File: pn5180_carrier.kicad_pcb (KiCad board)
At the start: 2 copper layers, 62.5 x 106.5 mm, 35 parts, among them J1 Bay 0 (CLIK-Mate 1x10), J10 24V IN (CLIK-Mate 1x2), J2 Bay 1 (CLIK-Mate 1x10), J3 Bay 2 (CLIK-Mate 1x10), J4 Bay 3 (CLIK-Mate 1x10), J5 Bay 4 (CLIK-Mate 1x10), J6 Bay 5 (CLIK-Mate 1x10), J7 Bay 6 (CLIK-Mate 1x10), J8 Bay 7 (CLIK-Mate 1x10), U1 74HC138, U2 74HC151, U4 TLV1117LV33DCYR, U5 XIAO ESP32C6, U6 MP1584EN module (set 5.0V)

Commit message: PCB: J1-J8 swapped to the 2x5 CLIK-Mate footprint (Update PCB from Schematic, KiCad GUI)
Same positions and orientations as the 1x10 parts; tracks to the bay connectors
still need re-routing. Project file records schematic rev 1.4.

Co-Authored-By: Claude Fable 5.1 <noreply@anthropic.com>
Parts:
- J1: value Bay 0 (CLIK-Mate 1x10) -> Bay 0 (CLIK-Mate 2x5); footprint Connector_Molex:Molex_CLIK-Mate_502494-1070_1x10-1MP_P2.00mm_Horizontal -> carrier:Molex_CLIK-Mate_503148-1090_2x05-1MP_P1.50mm_Horizontal
- J2: value Bay 1 (CLIK-Mate 1x10) -> Bay 1 (CLIK-Mate 2x5); footprint Connector_Molex:Molex_CLIK-Mate_502494-1070_1x10-1MP_P2.00mm_Horizontal -> carrier:Molex_CLIK-Mate_503148-1090_2x05-1MP_P1.50mm_Horizontal
- J3: value Bay 2 (CLIK-Mate 1x10) -> Bay 2 (CLIK-Mate 2x5); footprint Connector_Molex:Molex_CLIK-Mate_502494-1070_1x10-1MP_P2.00mm_Horizontal -> carrier:Molex_CLIK-Mate_503148-1090_2x05-1MP_P1.50mm_Horizontal
- J4: value Bay 3 (CLIK-Mate 1x10) -> Bay 3 (CLIK-Mate 2x5); footprint Connector_Molex:Molex_CLIK-Mate_502494-1070_1x10-1MP_P2.00mm_Horizontal -> carrier:Molex_CLIK-Mate_503148-1090_2x05-1MP_P1.50mm_Horizontal
- J5: value Bay 4 (CLIK-Mate 1x10) -> Bay 4 (CLIK-Mate 2x5); footprint Connector_Molex:Molex_CLIK-Mate_502494-1070_1x10-1MP_P2.00mm_Horizontal -> carrier:Molex_CLIK-Mate_503148-1090_2x05-1MP_P1.50mm_Horizontal
- J6: value Bay 5 (CLIK-Mate 1x10) -> Bay 5 (CLIK-Mate 2x5); footprint Connector_Molex:Molex_CLIK-Mate_502494-1070_1x10-1MP_P2.00mm_Horizontal -> carrier:Molex_CLIK-Mate_503148-1090_2x05-1MP_P1.50mm_Horizontal
- J7: value Bay 6 (CLIK-Mate 1x10) -> Bay 6 (CLIK-Mate 2x5); footprint Connector_Molex:Molex_CLIK-Mate_502494-1070_1x10-1MP_P2.00mm_Horizontal -> carrier:Molex_CLIK-Mate_503148-1090_2x05-1MP_P1.50mm_Horizontal
- J8: value Bay 7 (CLIK-Mate 1x10) -> Bay 7 (CLIK-Mate 2x5); footprint Connector_Molex:Molex_CLIK-Mate_502494-1070_1x10-1MP_P2.00mm_Horizontal -> carrier:Molex_CLIK-Mate_503148-1090_2x05-1MP_P1.50mm_Horizontal
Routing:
- net MOSI: track 211.4 -> 114.7 mm, vias 12 -> 6
- net MISO: track 211.8 -> 300.3 mm, vias 12 -> 14
- net +3V3: track 426.7 -> 404.5 mm, vias 15 -> 10
- net BUSY5: track 36.8 -> 19.3 mm, vias 2 -> 1
- net +5V: track 437.4 -> 424.5 mm
- net NSS5: track 16.5 -> 8.94 mm, vias 2 -> 0
- net ~{RST}: track 246.5 -> 241.3 mm, vias 6 -> 4
- net SCK: track 193.3 -> 190.3 mm
- net GND: vias 43 -> 37

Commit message: 3D models for the parts KiCad ships none for; preview render and tools
- carrier.3dshapes/: simplified VRML models generated by tools/gen_3d_models.py —
  CLIK-Mate 503148-1090 2x5 and 502494-0270 1x2 receptacles, XIAO ESP32C6 on its two
  8.5 mm sockets (rounded board, castellations, USB-C, shield, u.FL, chip antenna,
  buttons), MP1584EN module, Littelfuse NANO2 fuse
- carrier.pretty: model references on the three custom footprints; project-local
  copies of the stock J10 and F1 footprints that differ only in the model path;
  schematic/BOM/README point J10 and F1 at carrier:
- PCB: model references text-patched into the embedded footprints (all 35 resolve);
  otherwise identical to the owner's a606ea7 save
- tools/: footprint and model generators, render_3d_preview.py (kicad-cli pcb render on
  a temp copy); pn5180_carrier_3d_preview.png; renders/ ignored
- README/CLAUDE.md/MEMORY.md: files, tooling, conventions, PCB status, item 13

Co-Authored-By: Claude Fable 5.1 <noreply@anthropic.com>
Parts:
- F1: footprint Fuse:Fuse_Littelfuse-NANO2-451_453 -> carrier:Fuse_Littelfuse-NANO2-451_453
- J10: footprint Connector_Molex:Molex_CLIK-Mate_502494-0270_1x02-1MP_P2.00mm_Horizontal -> carrier:Molex_CLIK-Mate_502494-0270_1x02-1MP_P2.00mm_Horizontal
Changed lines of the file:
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@@
 		)
 		(embedded_fonts no)
+		(model "${KIPRJMOD}/carrier.3dshapes/Molex_CLIK-Mate_503148-1090_2x05_RA.wrl"
+			(offset
+				(xyz 0 0 0)
+			)
+			(scale
+				(xyz 1 1 1)
+			)
+			(rotate
+				(xyz 0 0 0)
+			)
+		)
 	)
 	(footprint "Diode_SMD:D_SOD-128"
@@
 		)
 		(embedded_fonts no)
+		(model "${KIPRJMOD}/carrier.3dshapes/Seeed_XIAO_ESP32C6_on_2x7_sockets.wrl"
+			(offset
+				(xyz 0 0 0)
+			)
+			(scale
+				(xyz 1 1 1)
+			)
+			(rotate
+				(xyz 0 0 0)
+			)
+		)
 	)
 	(footprint "Capacitor_SMD:C_1210_3225Metric_Pad1.33x2.70mm_HandSolder"
@@
 		)
 		(embedded_fonts no)
+		(model "${KIPRJMOD}/carrier.3dshapes/Molex_CLIK-Mate_503148-1090_2x05_RA.wrl"
+			(offset
+				(xyz 0 0 0)
+			)
+			(scale
+				(xyz 1 1 1)
+			)
+			(rotate
+				(xyz 0 0 0)
+			)
+		)
 	)
 	(footprint "carrier:Molex_CLIK-Mate_503148-1090_2x05-1MP_P1.50mm_Horizontal"
@@
 		)
 		(embedded_fonts no)
+		(model "${KIPRJMOD}/carrier.3dshapes/Molex_CLIK-Mate_503148-1090_2x05_RA.wrl"
+			(offset
+				(xyz 0 0 0)
+			)
+			(scale
+				(xyz 1 1 1)
+			)
+			(rotate
+				(xyz 0 0 0)
+			)
+		)
 	)
-	(footprint "Fuse:Fuse_Littelfuse-NANO2-451_453"
+	(footprint "carrier:Fuse_Littelfuse-NANO2-451_453"
 		(layer "F.Cu")
 		(at 135.5 144 180)
@@
 		)
 		(embedded_fonts no)
-		(model "${KICAD10_3DMODEL_DIR}/Fuse.3dshapes/Fuse_Littelfuse-NANO2-451_453.step"
+		(model "${KIPRJMOD}/carrier.3dshapes/Littelfuse_NANO2_451_453.wrl"
 			(offset
 				(xyz 0 0 0)
@@
 		)
 		(embedded_fonts no)
+		(model "${KIPRJMOD}/carrier.3dshapes/Molex_CLIK-Mate_503148-1090_2x05_RA.wrl"
+			(offset
+				(xyz 0 0 0)
+			)
+			(scale
+				(xyz 1 1 1)
+			)
+			(rotate
+				(xyz 0 0 0)
+			)
+		)
 	)
 	(footprint "Package_SO:SOIC-16_3.9x9.9mm_P1.27mm"
@@
 		)
 		(embedded_fonts no)
+		(model "${KIPRJMOD}/carrier.3dshapes/Molex_CLIK-Mate_503148-1090_2x05_RA.wrl"
+			(offset
+				(xyz 0 0 0)
+			)
+			(scale
+				(xyz 1 1 1)
+			)
+			(rotate
+				(xyz 0 0 0)
+			)
+		)
 	)
 	(footprint "carrier:Molex_CLIK-Mate_503148-1090_2x05-1MP_P1.50mm_Horizontal"
@@
 		)
 		(embedded_fonts no)
+		(model "${KIPRJMOD}/carrier.3dshapes/Molex_CLIK-Mate_503148-1090_2x05_RA.wrl"
+			(offset
+				(xyz 0 0 0)
+			)
+			(scale
+				(xyz 1 1 1)
+			)
+			(rotate
+				(xyz 0 0 0)
+			)
+		)
 	)
 	(footprint "carrier:Molex_CLIK-Mate_503148-1090_2x05-1MP_P1.50mm_Horizontal"
@@
 		)
 		(embedded_fonts no)
+		(model "${KIPRJMOD}/carrier.3dshapes/Molex_CLIK-Mate_503148-1090_2x05_RA.wrl"
+			(offset
+				(xyz 0 0 0)
+			)
+			(scale
+				(xyz 1 1 1)
+			)
+			(rotate
+				(xyz 0 0 0)
+			)
+		)
 	)
-	(footprint "Connector_Molex:Molex_CLIK-Mate_502494-0270_1x02-1MP_P2.00mm_Horizontal"
+	(footprint "carrier:Molex_CLIK-Mate_502494-0270_1x02-1MP_P2.00mm_Horizontal"
 		(layer "F.Cu")
 		(at 139.8825 154)
@@
 		)
 		(embedded_fonts no)
-		(model "${KICAD10_3DMODEL_DIR}/Connector_Molex.3dshapes/Molex_CLIK-Mate_502494-0270_1x02-1MP_P2.00mm_Horizontal.step"
+		(model "${KIPRJMOD}/carrier.3dshapes/Molex_CLIK-Mate_502494-0270_1x02_RA.wrl"
 			(offset
 				(xyz 0 0 0)
@@
 		)
 		(embedded_fonts no)
+		(model "${KIPRJMOD}/carrier.3dshapes/Molex_CLIK-Mate_503148-1090_2x05_RA.wrl"
+			(offset
+				(xyz 0 0 0)
+			)
+			(scale
+				(xyz 1 1 1)
+			)
+			(rotate
+				(xyz 0 0 0)
+			)
+		)
 	)
 	(footprint "Package_SO:SOIC-16_3.9x9.9mm_P1.27mm"
@@
 		)
 		(embedded_fonts no)
+		(model "${KIPRJMOD}/carrier.3dshapes/MP1584EN_Module_22x17.wrl"
+			(offset
+				(xyz 0 0 0)
+			)
+			(scale
+				(xyz 1 1 1)
+			)
+			(rotate
+				(xyz 0 0 0)
+			)
+		)
 	)
 	(footprint "Resistor_SMD:R_0603_1608Metric_Pad0.98x0.95mm_HandSolder"

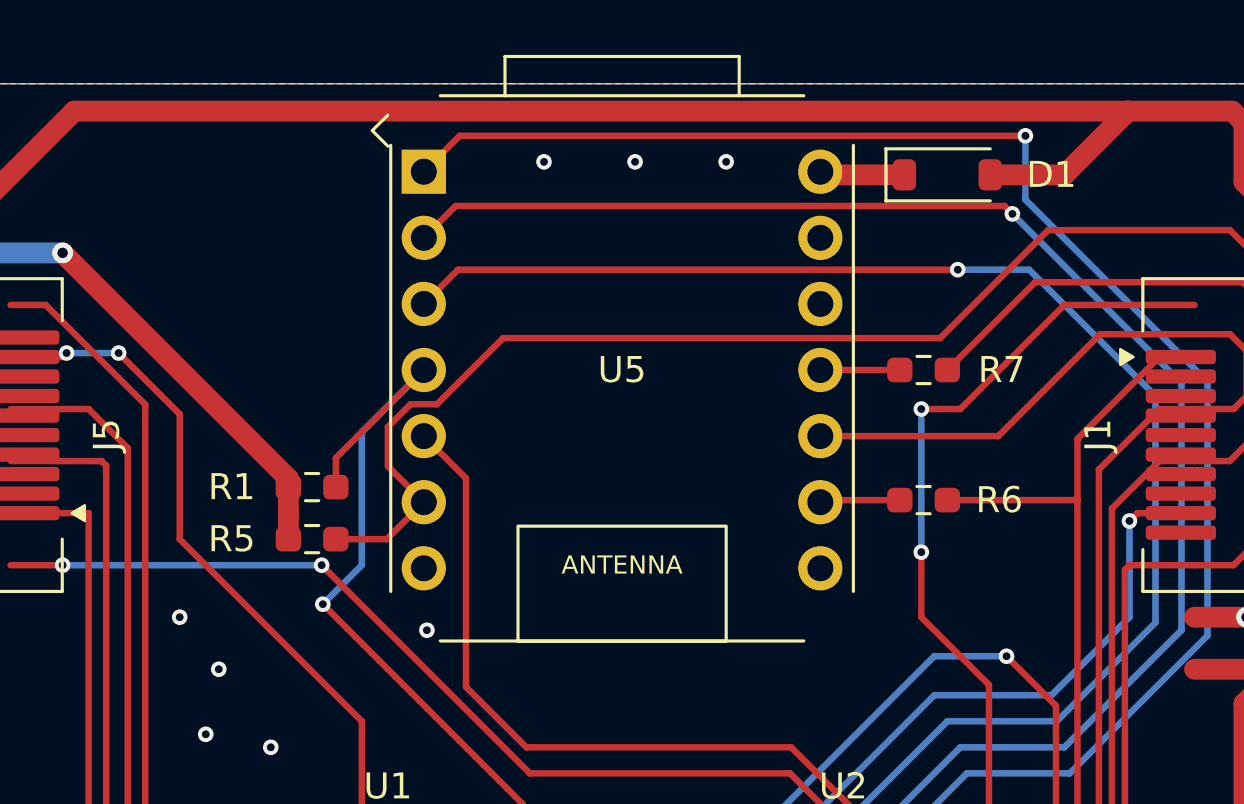
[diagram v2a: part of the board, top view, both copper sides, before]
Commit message: XIAO soldered flat (castellated SMD footprint), photo-accurate XIAO and MP1584EN models
- carrier.pretty/Seeed_XIAO_ESP32C6_SMD (tools/gen_xiao_smd_fp.py): 14 pads 1.5x2.5 at
  2.54 mm on the module edges, same 1-14 numbering; U5 switched in the schematic, BOM
  and (by script, same position/nets/fields) on the PCB; the Wuerth sockets leave the
  Mouser order list. Tracks to U5 end 1.27 mm short of the new pads (re-route).
- 3D: XIAO rebuilt from the owner's photos (rounded board, half-hole castellations,
  USB-C over the edge, R/B buttons and LEDs, white shield, u.FL, chip antenna), flat and
  socketed variants; MP1584EN per the owner's photo (black PCB, shielded inductor,
  SOIC-8, ceramics, diode, plated corner holes, no trimmer); J10 on the stock F.Fab
  outline; fuse model.
- Docs: sockets removed everywhere, post-swap DRC numbers (zones saved unfilled: refill
  before quoting DRC), stock-footprint list now nine names, stale "PCB not yet updated"
  fixed, open items 12/14, fuse wording aligned between BOM CSV and README.

Co-Authored-By: Claude Fable 5.1 <noreply@anthropic.com>
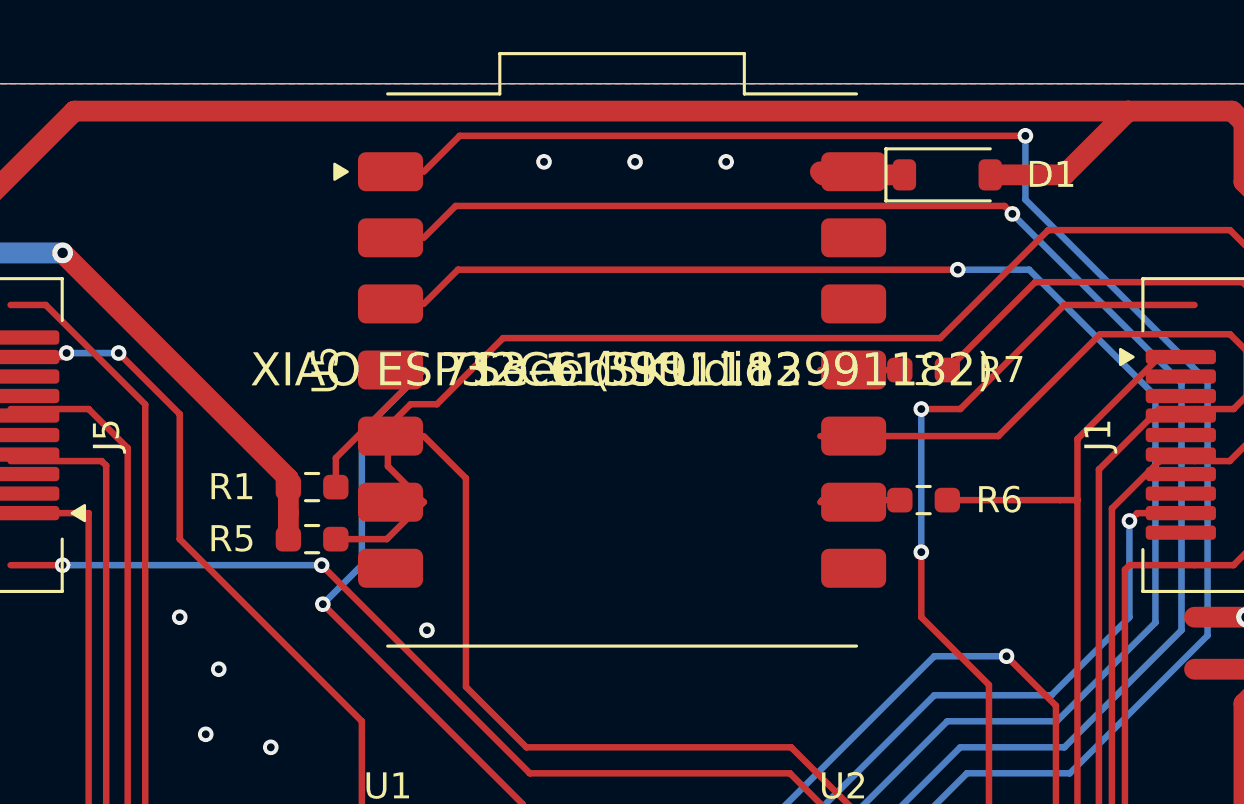
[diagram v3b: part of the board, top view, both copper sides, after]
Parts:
- U5: footprint carrier:Seeed_XIAO_2x7_Socket -> carrier:Seeed_XIAO_ESP32C6_SMD

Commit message: PCB: owner's routing session saved at 12:15 (KiCad GUI)
Co-Authored-By: Claude Fable 5.1 <noreply@anthropic.com>
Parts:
- moved D1 1.00 mm to (153.5, 55.5)
- moved R6 0.91 mm to (152.5, 68.0)
- moved R7 0.91 mm to (152.5, 63.0)
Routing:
- net MISO: track 300.3 -> 177.2 mm, vias 14 -> 4
- net NSS7: track 77.2 -> 156.4 mm
- net ~{RST}: track 241.3 -> 198.4 mm, vias 4 -> 1
- net MOSI: track 114.7 -> 88.1 mm, vias 6 -> 3
- net SCK: track 190.3 -> 167.1 mm, vias 6 -> 3
- net +3V3: track 404.5 -> 393.6 mm, vias 10 -> 5
- net BUSY6: track 59.1 -> 50.6 mm, vias 4 -> 3
- net BUSY3: track 61.9 -> 54.9 mm, vias 2 -> 0
- net NSS6: track 43.4 -> 37.4 mm, vias 2 -> 0
- net NSS3: track 118.1 -> 112.1 mm, vias 4 -> 2
- net NSS0: track 47.0 -> 44.4 mm, vias 2 -> 1
- net NSS4: track 30.7 -> 28.5 mm, vias 2 -> 1
- net NSS1: track 38.9 -> 36.9 mm, vias 2 -> 1
- net BUSY4: track 49.3 -> 47.3 mm, vias 2 -> 1
- net BUSY1: track 12.2 -> 10.2 mm, vias 2 -> 1
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
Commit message: U6 is the fixed-5 V module: strip the pot-setting text; align U5/F1 fields
- U6: Value "MP1584EN module, fixed 5V", Description and library ki_description say
  fixed 5V output (no trimmer); DESIGN NOTES line, BOM CSV, README §buck and BOM row
  reworded; CLAUDE.md open item 9 resolved, MEMORY.md item 7 and open question closed.
- U5: MPN "XIAO ESP32C6" in the schematic to match the owner's shortened PCB silk
  field (SKU 113991182 moved into Description) — DRC parity back to 0; Description
  and the two DESIGN NOTES lines now say soldered flat on 14 castellations, no sockets.
- F1: Value "1A", Description "NANO2 451/453 (fast-acting series)" in schematic and PCB.
- Re-exported schematic PDF/PNG. Checks: netlist 38/189/0, ERC 82 (unchanged),
  DRC parity 0; refilled DRC on the owner's 12:15 save is 170/89 (logged in MEMORY.md).

Co-Authored-By: Claude Fable 5.1 <noreply@anthropic.com>
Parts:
- F1: value 1A slow -> 1A
- U6: value MP1584EN module (set 5.0V) -> MP1584EN module, fixed 5V
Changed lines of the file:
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@@
 			)
 		)
-		(property "Value" "1A slow"
+		(property "Value" "1A"
 			(at 0 2.7 180)
 			(unlocked yes)
@@
 			)
 		)
-		(property "Description" "1A slow-blow SMD fuse, NANO2"
+		(property "Description" "1A SMD fuse, NANO2 451/453 (fast-acting series; see CLAUDE.md open item 13)"
 			(at 0 0 180)
 			(unlocked yes)
@@
 			)
 		)
-		(property "Description" "XIAO ESP32C6 module, 2x7 pins on 15.24mm (user-supplied; verify Mouser #)"
+		(property "Description" "XIAO ESP32C6 module (Seeed SKU 113991182), soldered flat on its 14 castellations (user-supplied; verify Mouser #)"
 			(at 0 0 90)
 			(layer "F.Fab")
@@
 			)
 		)
-		(property "Value" "MP1584EN module (set 5.0V)"
+		(property "Value" "MP1584EN module, fixed 5V"
 			(at 0 10 90)
 			(layer "F.Fab")
@@
 			)
 		)
-		(property "Description" "22x17mm adjustable module, user-supplied (Amazon); set to 5.0V"
+		(property "Description" "22x17mm fixed-5V module (no trimmer), user-supplied (Amazon)"
 			(at 0 0 90)
 			(layer "F.Fab")
